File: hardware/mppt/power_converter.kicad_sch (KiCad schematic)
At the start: 4 parts, among them J301 CT3151, J302 CT3151, J303 CT3151, J304 CT3151

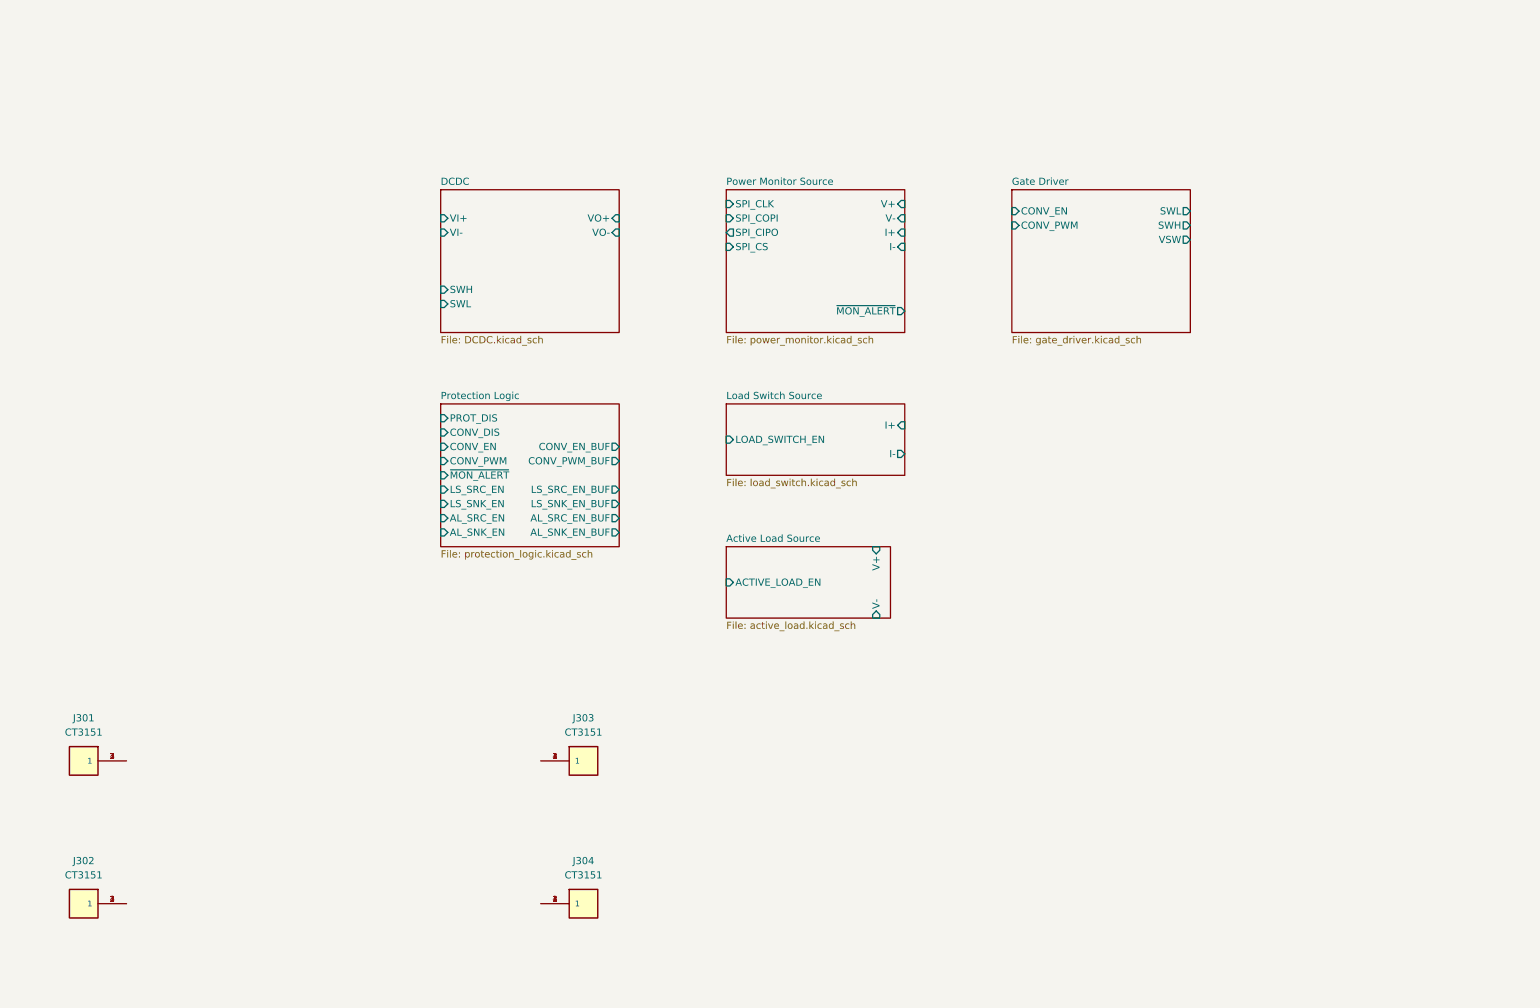
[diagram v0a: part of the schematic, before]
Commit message: run through mppt sch, going through bom
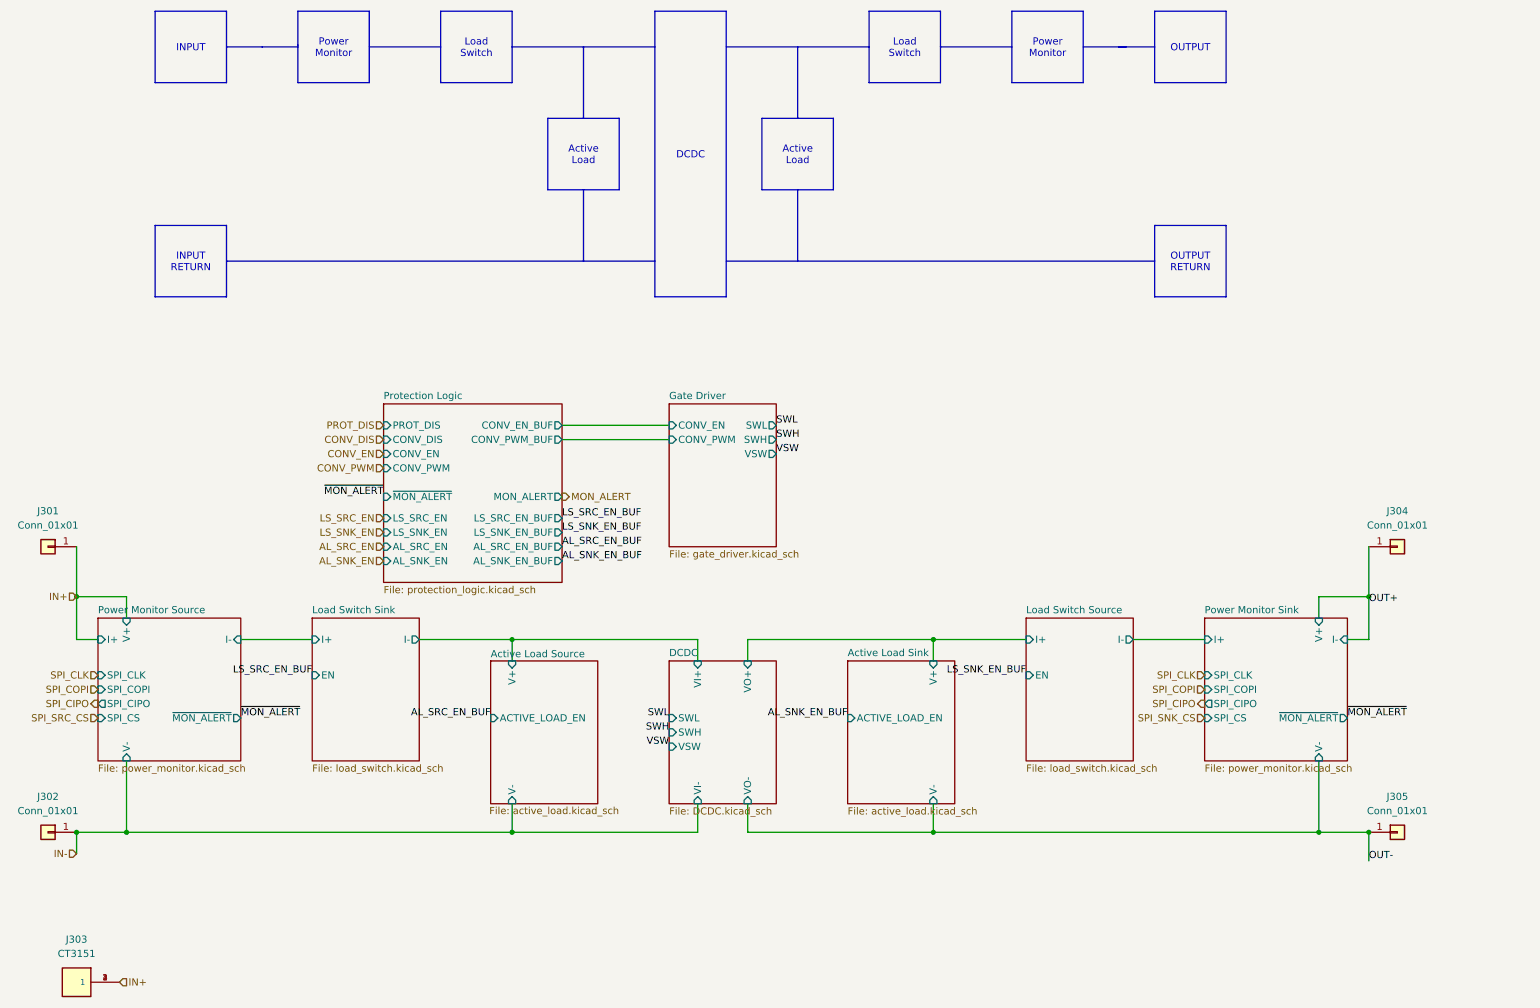
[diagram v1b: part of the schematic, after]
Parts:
- removed J301, J302, J304: CT3151, footprints:caltest_ct3151, symbol caltest_ct3151:CT3151
- added J301, J302, J304, J305: Conn_01x01, symbol Connector_Generic:Conn_01x01
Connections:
- net IN+: now reaches J303.1, J303.2 (1), J303.3 (1), J303.4 (1)
- net IN+: now also J301.1 (Pin_1)
- new net IN-: J302.1 (Pin_1)
- new net OUT+: J304.1 (Pin_1)
- new net OUT-: J305.1 (Pin_1)
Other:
- added sheet Active Load Sink (active_load.kicad_sch)
- added sheet Load Switch Sink (load_switch.kicad_sch)
- added sheet Power Monitor Sink (power_monitor.kicad_sch)
- sheet DCDC ports: added VSW; removed none
- sheet Load Switch Source ports: added EN; removed LOAD_SWITCH_EN
- sheet Protection Logic ports: added MON_ALERT; removed none

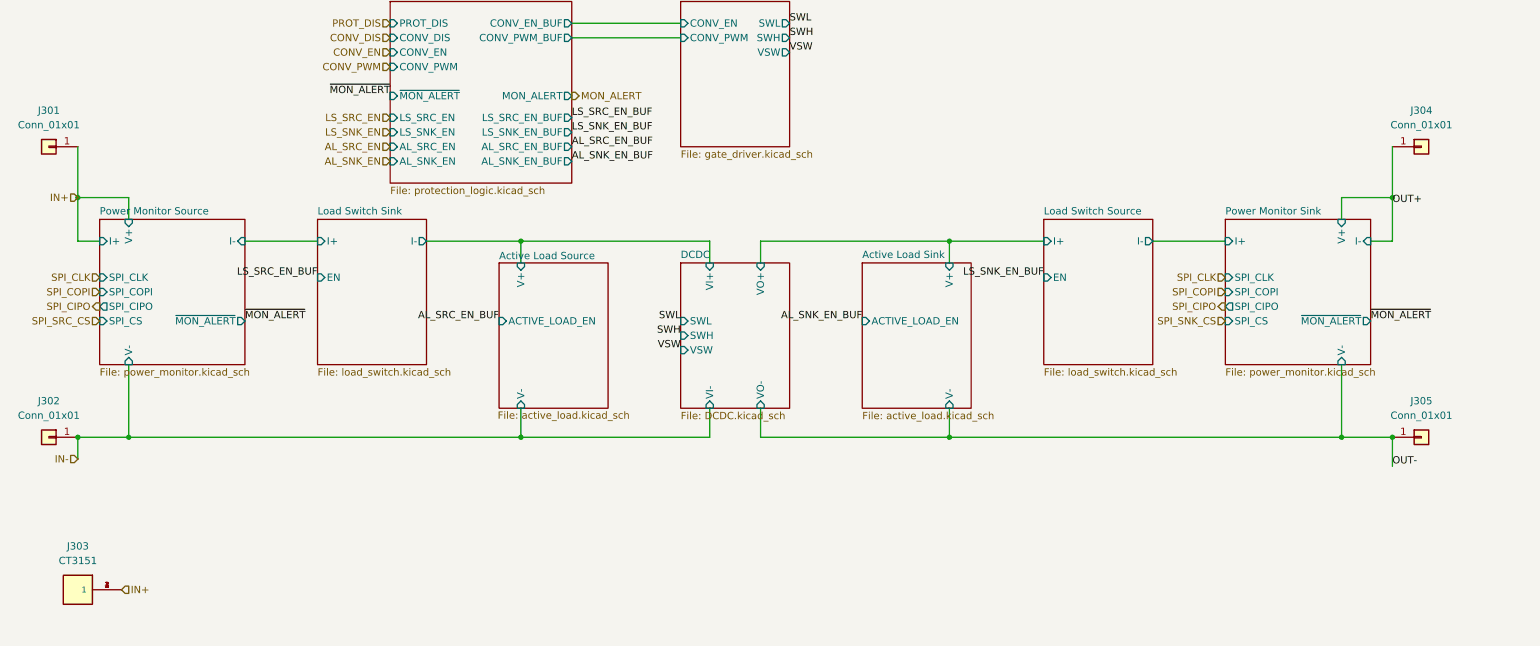
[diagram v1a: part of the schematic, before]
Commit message: update final missing pieces for sch, moving to bom pop
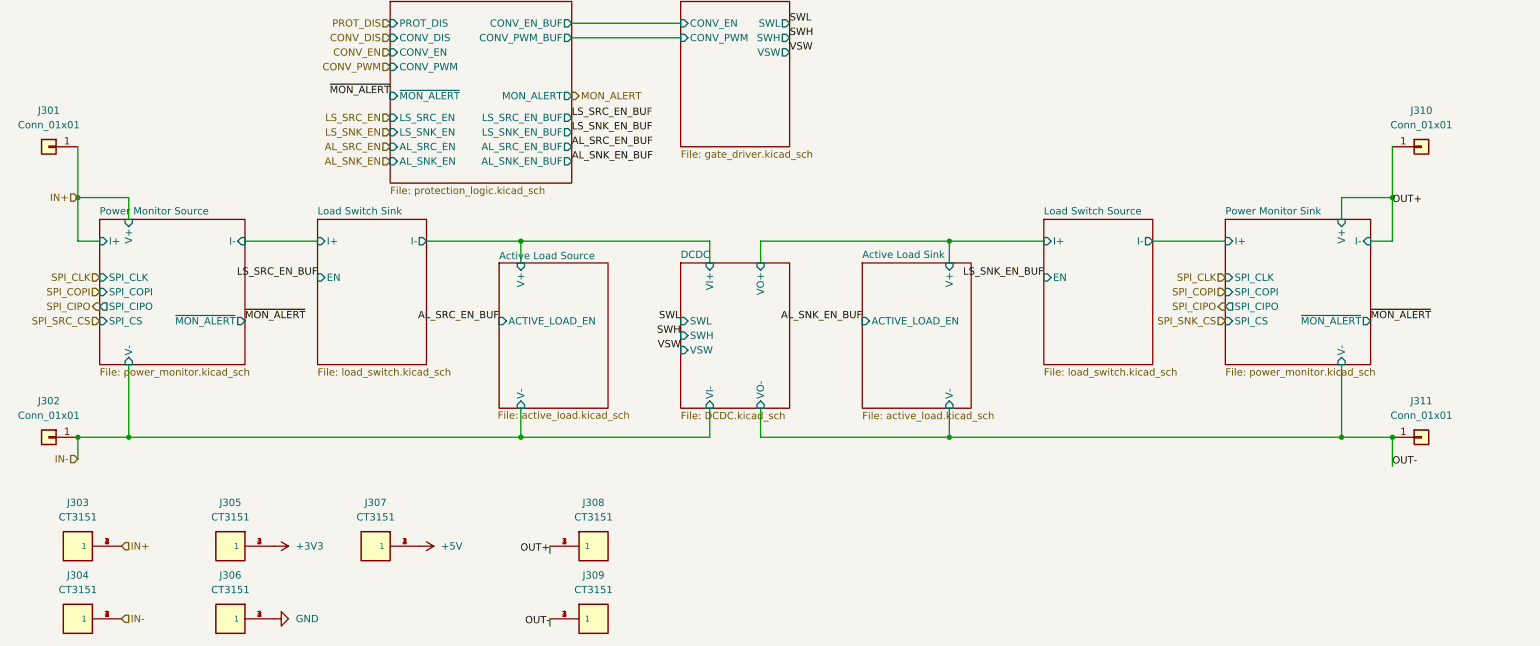
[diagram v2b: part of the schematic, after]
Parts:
- added J304, J305, J306, J307, J308, J309: CT3151, footprints:caltest_ct3151, symbol caltest_ct3151:CT3151
- renumbered J304 to J310, J305 to J311
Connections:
- net IN-: now also J304.1, J304.2 (1), J304.3 (1), J304.4 (1)
- net OUT+: now also J308.1, J308.2 (1), J308.3 (1), J308.4 (1)
- net OUT-: now also J309.1, J309.2 (1), J309.3 (1), J309.4 (1)
- new net +3V3: J305.1, J305.2 (1), J305.3 (1), J305.4 (1)
- new net +5V: J307.1, J307.2 (1), J307.3 (1), J307.4 (1)
- new net GND: J306.1, J306.2 (1), J306.3 (1), J306.4 (1)

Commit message: bom consolidated, starting layout
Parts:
- removed J305, J306, J307: CT3151, footprints:caltest_ct3151, symbol caltest_ct3151:CT3151
- added TP301, TP302, TP303: TestPoint, TestPoint:TestPoint_Keystone_5000-5004_Miniature, symbol Connector:TestPoint
- J301, J302: footprint (none) -> footprints:ke_7771_SEMS; Manufacturer (none) -> Keystone Electronics; P/N (none) -> 7771-SEMS
- J307: renamed from J310; footprint (none) -> footprints:ke_7771_SEMS; Manufacturer (none) -> Keystone Electronics; P/N (none) -> 7771-SEMS
- J308: renamed from J311; footprint (none) -> footprints:ke_7771_SEMS; Manufacturer (none) -> Keystone Electronics; P/N (none) -> 7771-SEMS
- renumbered J308 to J305, J309 to J306
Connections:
- net +3V3: now also TP303.1
- net +5V: now also TP301.1
- net GND: now also TP302.1

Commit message: progress on layout
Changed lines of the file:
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@@
 	)
 	(junction
-		(at 254 123.19)
-		(diameter 0)
-		(color 0 0 0 0)
-	)
-	(junction
-		(at 24.13 123.19)
+		(at 24.13 165.1)
 		(diameter 0)
 		(color 0 0 0 0)
 	)
 	(junction
-		(at 24.13 165.1)
+		(at 101.6 165.1)
 		(diameter 0)
 		(color 0 0 0 0)
 	)
 	(junction
-		(at 101.6 165.1)
+		(at 222.25 130.81)
 		(diameter 0)
 		(color 0 0 0 0)
@@
 		(color 0 0 0 0)
 	)
+	(junction
+		(at 55.88 130.81)
+		(diameter 0)
+		(color 0 0 0 0)
+	)
 	(wire
 		(pts
-			(xy 212.09 130.81) (xy 224.79 130.81)
+			(xy 212.09 130.81) (xy 222.25 130.81)
 		)
 		(stroke
@@
 	(wire
 		(pts
-			(xy 245.11 127) (xy 245.11 123.19)
-		)
-		(stroke
-			(width 0)
-			(type default)
-		)
-	)
-	(wire
-		(pts
 			(xy 134.62 165.1) (xy 101.6 165.1)
 		)
@@
 	(wire
 		(pts
-			(xy 143.51 134.62) (xy 143.51 130.81)
+			(xy 222.25 128.27) (xy 222.25 130.81)
 		)
 		(stroke
@@
 		)
 	)
-	(polyline
+	(wire
 		(pts
-			(xy 139.7 63.5) (xy 215.9 63.5)
+			(xy 143.51 134.62) (xy 143.51 130.81)
 		)
 		(stroke
@@
 		)
 	)
-	(wire
+	(polyline
 		(pts
-			(xy 254 123.19) (xy 254 114.3)
+			(xy 139.7 63.5) (xy 215.9 63.5)
 		)
 		(stroke
@@
 	(wire
 		(pts
-			(xy 254 123.19) (xy 254 130.81)
-		)
-		(stroke
-			(width 0)
-			(type default)
-		)
-	)
-	(wire
-		(pts
 			(xy 27.94 130.81) (xy 24.13 130.81)
 		)
@@
 		)
 	)
-	(wire
-		(pts
-			(xy 24.13 114.3) (xy 24.13 123.19)
-		)
-		(stroke
-			(width 0)
-			(type default)
-		)
-	)
 	(polyline
 		(pts
@@
 	(wire
 		(pts
-			(xy 53.34 130.81) (xy 66.04 130.81)
+			(xy 53.34 130.81) (xy 55.88 130.81)
 		)
 		(stroke
@@
 	(wire
 		(pts
-			(xy 33.02 123.19) (xy 24.13 123.19)
+			(xy 250.19 130.81) (xy 254 130.81)
 		)
 		(stroke
@@
 	(wire
 		(pts
-			(xy 250.19 130.81) (xy 254 130.81)
+			(xy 24.13 114.3) (xy 24.13 130.81)
 		)
 		(stroke
@@
 		)
 	)
+	(wire
+		(pts
+			(xy 254 114.3) (xy 254 130.81)
+		)
+		(stroke
+			(width 0)
+			(type default)
+		)
+	)
 	(polyline
 		(pts
@@
 		)
 	)
+	(wire
+		(pts
+			(xy 55.88 130.81) (xy 66.04 130.81)
+		)
+		(stroke
+			(width 0)
+			(type default)
+		)
+	)
 	(polyline
 		(pts
@@
 	(wire
 		(pts
-			(xy 245.11 123.19) (xy 254 123.19)
+			(xy 24.13 165.1) (xy 33.02 165.1)
 		)
 		(stroke
@@
 	(wire
 		(pts
-			(xy 24.13 165.1) (xy 33.02 165.1)
+			(xy 222.25 130.81) (xy 224.79 130.81)
 		)
 		(stroke
@@
 	(wire
 		(pts
-			(xy 24.13 130.81) (xy 24.13 123.19)
+			(xy 53.34 128.27) (xy 55.88 128.27)
 		)
 		(stroke
@@
 	(wire
 		(pts
+			(xy 224.79 128.27) (xy 222.25 128.27)
+		)
+		(stroke
+			(width 0)
+			(type default)
+		)
+	)
+	(wire
+		(pts
 			(xy 143.51 160.02) (xy 143.51 165.1)
 		)
@@
 	(wire
 		(pts
-			(xy 176.53 130.81) (xy 176.53 134.62)
+			(xy 55.88 128.27) (xy 55.88 130.81)
 		)
 		(stroke
@@
 	(wire
 		(pts
-			(xy 33.02 127) (xy 33.02 123.19)
+			(xy 176.53 130.81) (xy 176.53 134.62)
 		)
 		(stroke
@@
 	)
 	(label "OUT+"
-		(at 254 124.46 0)
+		(at 254 114.3 180)
 		(fields_autoplaced yes)
 		(effects
@@
 				(size 1.27 1.27)
 			)
-			(justify left bottom)
+			(justify right bottom)
 		)
 	)
@@
 	(hierarchical_label "IN+"
 		(shape input)
-		(at 24.13 123.19 180)
+		(at 24.13 114.3 0)
 		(fields_autoplaced yes)
 		(effects
@@
 				(size 1.27 1.27)
 			)
-			(justify right)
+			(justify left)
 		)
 	)
@@
 		)
 		(pin "V+" input
-			(at 33.02 127 90)
+			(at 53.34 128.27 0)
 			(effects
 				(font
@@
 		)
 		(pin "V+" input
-			(at 245.11 127 90)
+			(at 224.79 128.27 180)
 			(effects
 				(font
 					(size 1.27 1.27)
 				)
-				(justify right)
+				(justify left)
 			)
 		)

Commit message: PCB variant for power regulation breakout.
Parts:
- J301, J302, J303, J304, J305, J306, J307, J308, TP301, TP302, TP303: now not fitted; now left out of the parts list
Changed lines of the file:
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@@
 		(unit 1)
 		(exclude_from_sim no)
-		(in_bom yes)
-		(on_board yes)
-		(dnp no)
+		(in_bom no)
+		(on_board no)
+		(dnp yes)
 		(fields_autoplaced yes)
 		(property "Reference" "#PWR0302"
@@
 		(unit 1)
 		(exclude_from_sim no)
-		(in_bom yes)
-		(on_board yes)
-		(dnp no)
+		(in_bom no)
+		(on_board no)
+		(dnp yes)
 		(property "Reference" "J307"
 			(at 259.08 107.95 0)
@@
 		(unit 1)
 		(exclude_from_sim no)
-		(in_bom yes)
-		(on_board yes)
-		(dnp no)
+		(in_bom no)
+		(on_board no)
+		(dnp yes)
 		(fields_autoplaced yes)
 		(property "Reference" "J304"
@@
 		(unit 1)
 		(exclude_from_sim no)
-		(in_bom yes)
-		(on_board yes)
-		(dnp no)
+		(in_bom no)
+		(on_board no)
+		(dnp yes)
 		(fields_autoplaced yes)
 		(property "Reference" "#PWR0303"
@@
 		(unit 1)
 		(exclude_from_sim no)
-		(in_bom yes)
-		(on_board yes)
-		(dnp no)
+		(in_bom no)
+		(on_board no)
+		(dnp yes)
 		(fields_autoplaced yes)
 		(property "Reference" "TP301"
@@
 		(unit 1)
 		(exclude_from_sim no)
-		(in_bom yes)
-		(on_board yes)
-		(dnp no)
+		(in_bom no)
+		(on_board no)
+		(dnp yes)
 		(fields_autoplaced yes)
 		(property "Reference" "J305"
@@
 		(unit 1)
 		(exclude_from_sim no)
-		(in_bom yes)
-		(on_board yes)
-		(dnp no)
+		(in_bom no)
+		(on_board no)
+		(dnp yes)
 		(fields_autoplaced yes)
 		(property "Reference" "J301"
@@
 		(unit 1)
 		(exclude_from_sim no)
-		(in_bom yes)
-		(on_board yes)
-		(dnp no)
+		(in_bom no)
+		(on_board no)
+		(dnp yes)
 		(property "Reference" "J308"
 			(at 259.08 158.75 0)
@@
 		(unit 1)
 		(exclude_from_sim no)
-		(in_bom yes)
-		(on_board yes)
-		(dnp no)
+		(in_bom no)
+		(on_board no)
+		(dnp yes)
 		(property "Reference" "TP302"
 			(at 57.15 191.0081 0)
@@
 		(unit 1)
 		(exclude_from_sim no)
-		(in_bom yes)
-		(on_board yes)
-		(dnp no)
+		(in_bom no)
+		(on_board no)
+		(dnp yes)
 		(fields_autoplaced yes)
 		(property "Reference" "#PWR0301"
@@
 		(unit 1)
 		(exclude_from_sim no)
-		(in_bom yes)
-		(on_board yes)
-		(dnp no)
+		(in_bom no)
+		(on_board no)
+		(dnp yes)
 		(fields_autoplaced yes)
 		(property "Reference" "J302"
@@
 		(unit 1)
 		(exclude_from_sim no)
-		(in_bom yes)
-		(on_board yes)
-		(dnp no)
+		(in_bom no)
+		(on_board no)
+		(dnp yes)
 		(fields_autoplaced yes)
 		(property "Reference" "J306"
@@
 		(unit 1)
 		(exclude_from_sim no)
-		(in_bom yes)
-		(on_board yes)
-		(dnp no)
+		(in_bom no)
+		(on_board no)
+		(dnp yes)
 		(fields_autoplaced yes)
 		(property "Reference" "TP303"
@@
 		(unit 1)
 		(exclude_from_sim no)
-		(in_bom yes)
-		(on_board yes)
-		(dnp no)
+		(in_bom no)
+		(on_board no)
+		(dnp yes)
 		(fields_autoplaced yes)
 		(property "Reference" "J303"

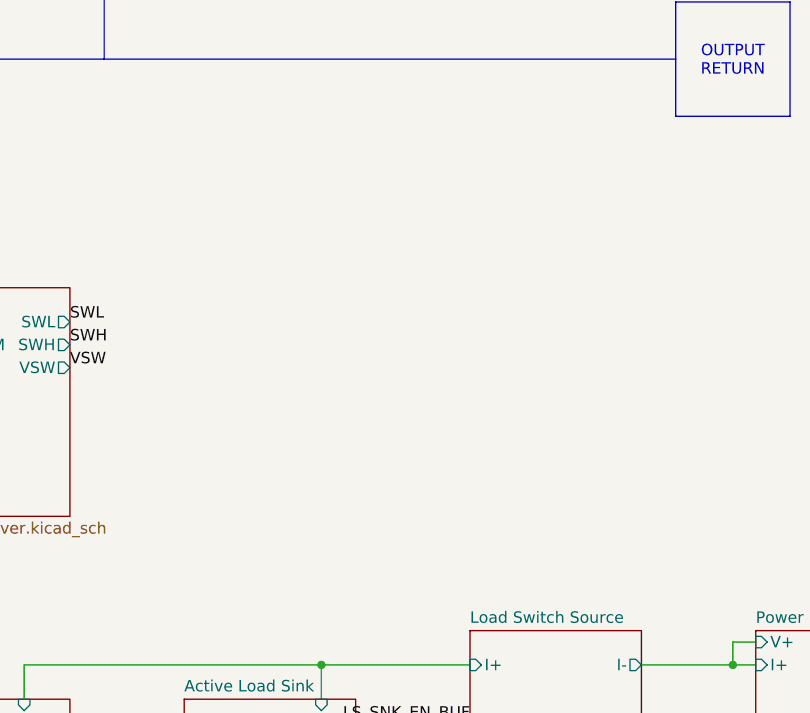
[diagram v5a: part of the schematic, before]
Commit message: complete layout, drc, signaling optimizations and added dnp testpoints
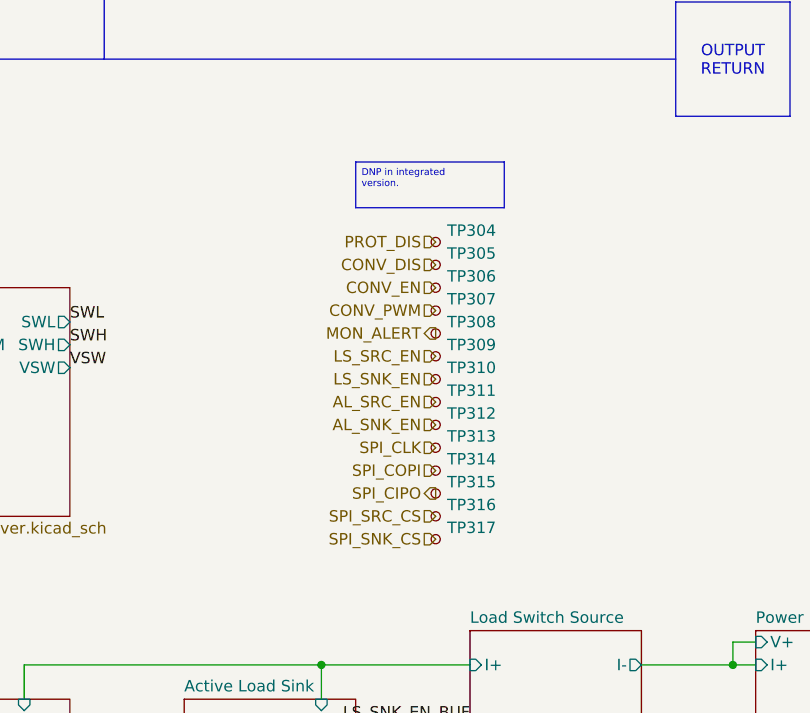
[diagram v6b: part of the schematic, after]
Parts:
- added TP304, TP305, TP306, TP307, TP308, TP309, TP310, TP311, TP312, TP313, TP314, TP315, TP316, TP317: TestPoint_Small, TestPoint:TestPoint_Pad_D1.0mm, symbol Connector:TestPoint_Small
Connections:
- net AL_SNK_EN: now also TP312.1
- net AL_SRC_EN: now also TP311.1
- net CONV_DIS: now also TP305.1
- net CONV_EN: now also TP306.1
- net CONV_PWM: now also TP307.1
- net LS_SNK_EN: now also TP310.1
- net LS_SRC_EN: now also TP309.1
- net MON_ALERT: now also TP308.1
- net PROT_DIS: now also TP304.1
- net SPI_CIPO: now also TP315.1
- net SPI_CLK: now also TP313.1
- net SPI_COPI: now also TP314.1
- net SPI_SNK_CS: now also TP317.1
- net SPI_SRC_CS: now also TP316.1
